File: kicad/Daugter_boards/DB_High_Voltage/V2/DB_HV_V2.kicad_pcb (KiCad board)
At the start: 2 copper layers, 40.6 x 50.8 mm, 6 parts, among them P1 CONN_01X19, P2 CONN_01X02, P3 CONN_01X19, P4 SMA, U1 R05-100B

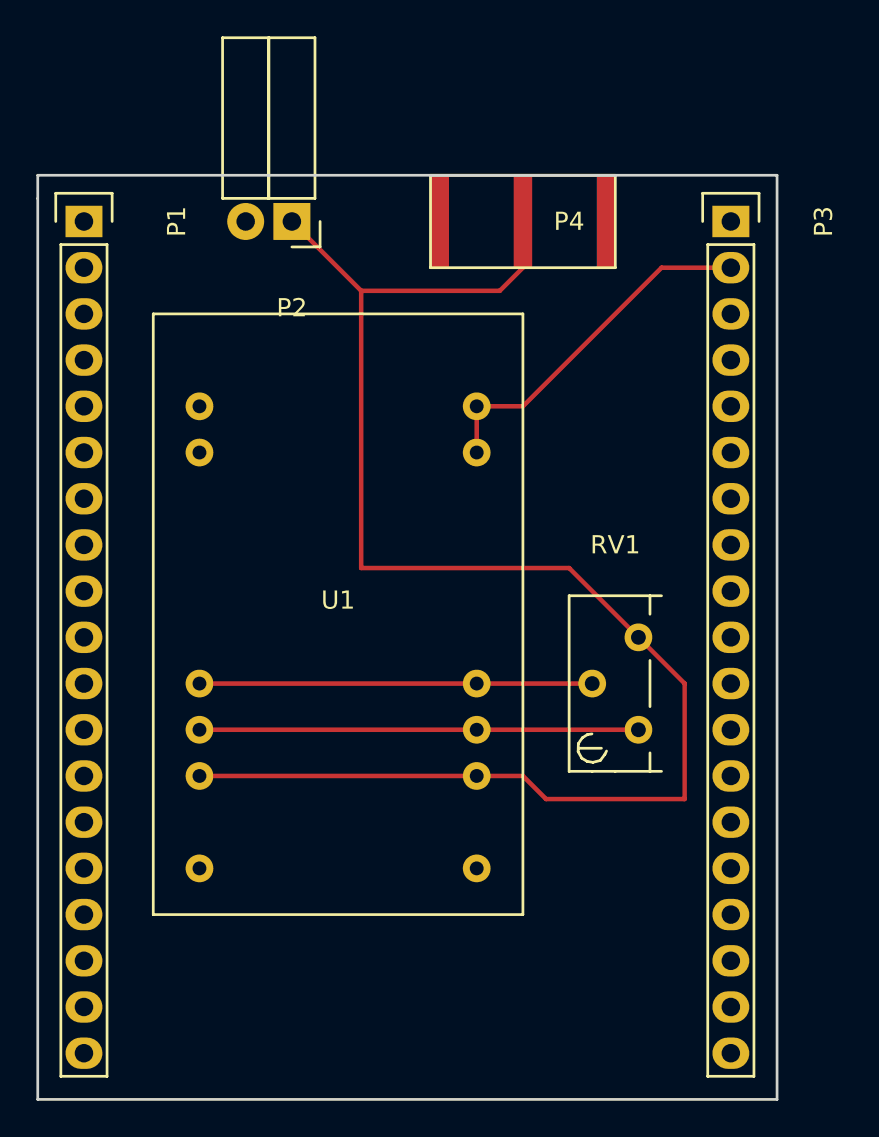
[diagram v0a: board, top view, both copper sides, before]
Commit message: inverting SMA layer position and improve finish of DB_HV
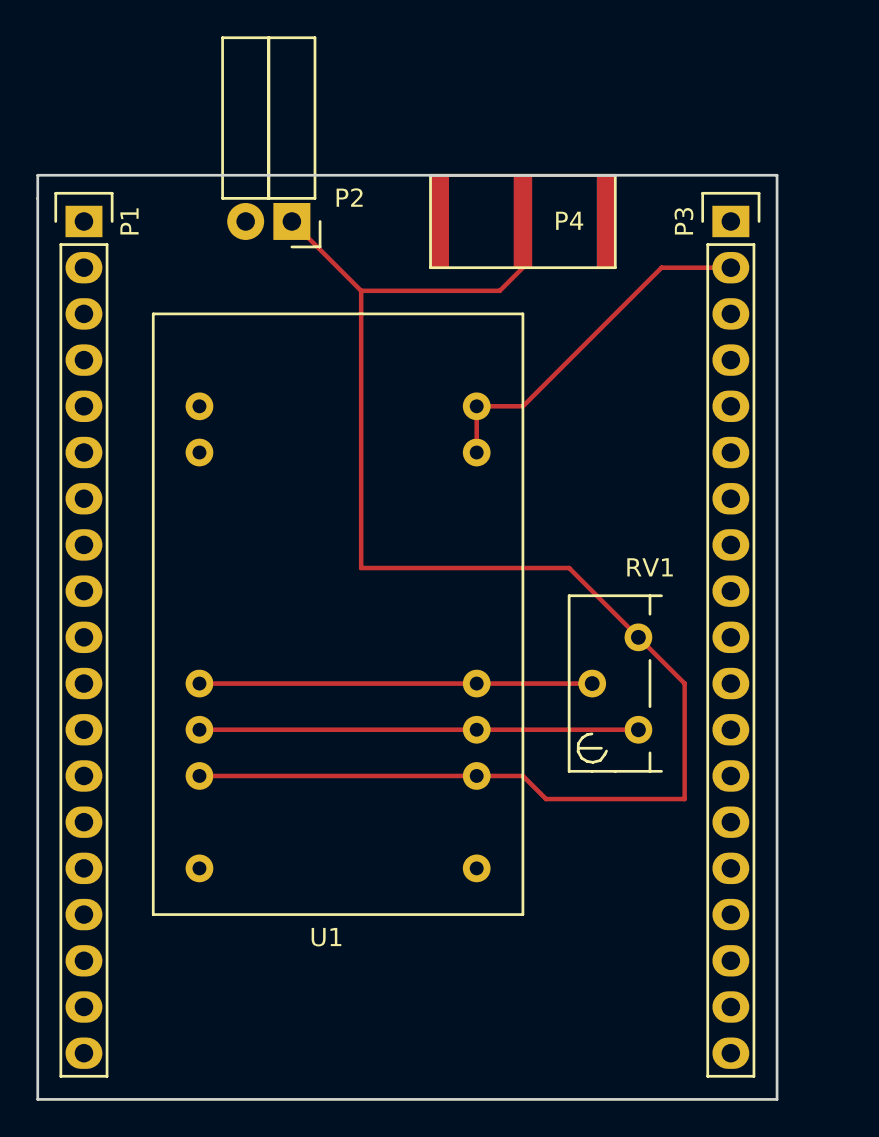
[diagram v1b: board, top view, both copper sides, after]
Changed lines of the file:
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@@
     (descr "Through hole socket strip")
     (tags "socket strip")
-    (fp_text reference P1 (at 0 -5.1 270) (layer F.SilkS)
+    (fp_text reference P1 (at 0 -2.54 270) (layer F.SilkS)
       (effects (font (size 1 1) (thickness 0.15)))
     )
@@
     (descr "Through hole socket strip")
     (tags "socket strip")
-    (fp_text reference P2 (at 0 -4.75 180) (layer F.SilkS)
+    (fp_text reference P2 (at -3.175 1.27 180) (layer F.SilkS)
       (effects (font (size 1 1) (thickness 0.15)))
     )
@@
     (descr "Through hole socket strip")
     (tags "socket strip")
-    (fp_text reference P3 (at 0 -5.1 270) (layer F.SilkS)
+    (fp_text reference P3 (at 0 2.54 270) (layer F.SilkS)
       (effects (font (size 1 1) (thickness 0.15)))
     )
@@
     (descr "3296, 3/8, Square, Trimpot, Trimming, Potentiometer, Bourns")
     (tags "3296, 3/8, Square, Trimpot, Trimming, Potentiometer, Bourns")
-    (fp_text reference RV1 (at -1.27 -10.16) (layer F.SilkS)
+    (fp_text reference RV1 (at 0.635 -8.89) (layer F.SilkS)
       (effects (font (size 1 1) (thickness 0.15)))
     )
@@
   (module echopen:RECOM (layer F.Cu)
     (at 72.39 68.58)
-    (fp_text reference U1 (at 0 0.5) (layer F.SilkS)
-      (effects (font (size 1 1) (thickness 0.15)))
-    )
+    (fp_text reference U1 (at -0.635 19.05) (layer F.SilkS)
+      (effects (font (size 1 1) (thickness 0.15)))
+    )

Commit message: correct non connected pin on DB_HV
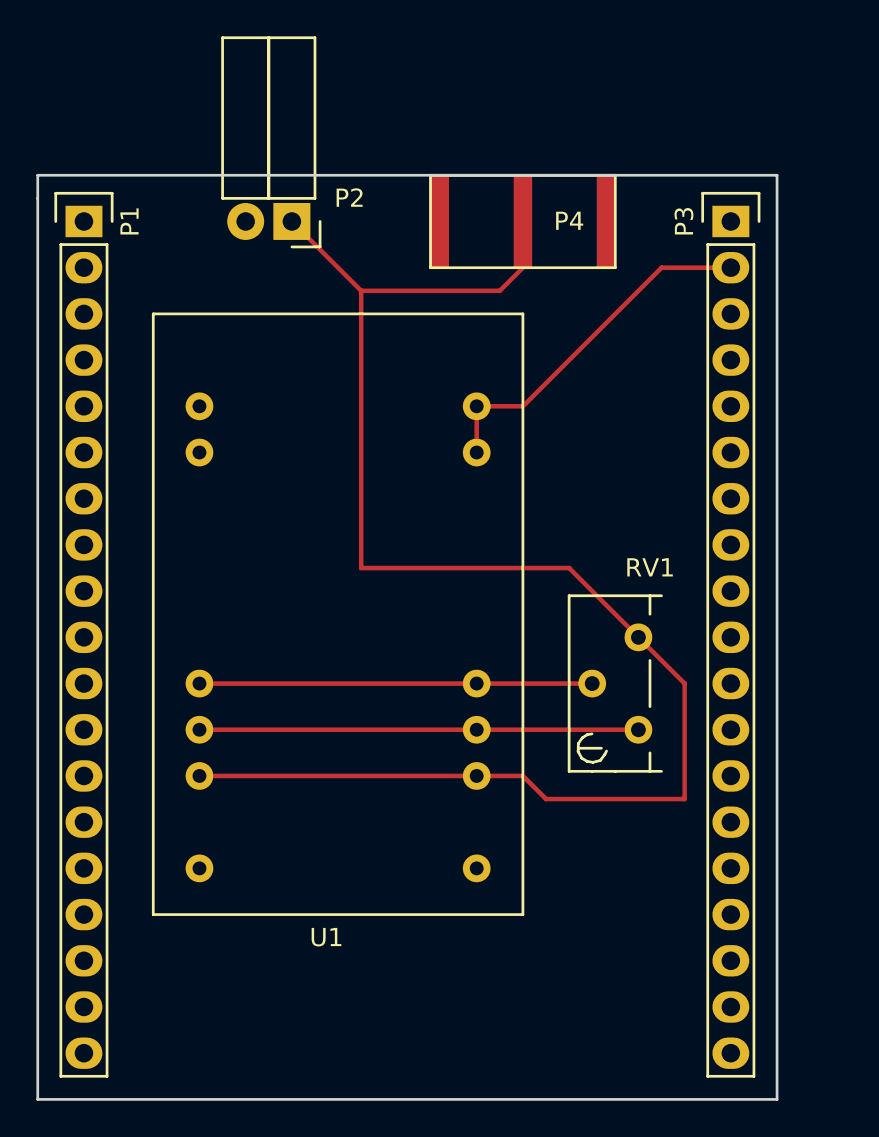
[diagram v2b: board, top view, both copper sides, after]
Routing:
- added copper zone on B.Cu, net GND
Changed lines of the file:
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@@
   (general
     (links 20)
-    (no_connects 2)
-    (area 55.804999 37.434999 100.155 96.595001)
+    (no_connects 0)
+    (area 55.804999 37.434999 98.155 96.595001)
     (thickness 1.6)
     (drawings 5)
@@
     (connect_pads (clearance 0.508))
     (min_thickness 0.254)
+    (fill yes (arc_segments 16) (thermal_gap 0.508) (thermal_bridge_width 0.508))
+    (polygon
+      (pts
+        (xy 96.52 96.52) (xy 55.88 96.52) (xy 55.88 45.72) (xy 96.52 45.72)
+      )
+    )
+  )
+  (zone (net 1) (net_name GND) (layer B.Cu) (hatch edge 0.508)
+    (connect_pads (clearance 0.508))
+    (min_thickness 0.254)
